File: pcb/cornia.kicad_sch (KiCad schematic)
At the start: 148 parts, among them J1 MJ-4PP-9, J2 OLED, J3 MJ-4PP-9, J4 OLED, SW1 SW_PUSH, SW10 SW_PUSH, SW11 SW_PUSH, SW12 SW_PUSH, SW13 SW_PUSH, SW14 SW_PUSH, SW15 SW_PUSH, SW16 SW_PUSH, SW17 SW_PUSH, SW18 SW_PUSH, SW19 SW_PUSH, SW2 SW_PUSH, SW20 SW_PUSH, SW21 SW_PUSH, SW22 SW_PUSH, SW23 SW_PUSH, SW24 SW_PUSH, SW25 SW_PUSH, SW26 SW_PUSH, SW27 SW_PUSH, SW28 SW_PUSH, SW29 SW_PUSH, SW3 SW_PUSH, SW30 SW_PUSH, SW31 SW_PUSH, SW32 SW_PUSH, SW33 SW_PUSH, SW34 SW_PUSH, SW35 SW_PUSH, SW36 SW_PUSH, SW37 SW_PUSH, SW38 SW_PUSH, SW39 SW_PUSH, SW4 SW_PUSH, SW40 SW_PUSH, SW41 SW_PUSH, SW42 SW_PUSH, SW5 SW_PUSH, SW6 SW_PUSH, SW7 SW_PUSH, SW8 SW_PUSH, SW9 SW_PUSH, U1 ProMicro, U2 ProMicro

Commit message: First push V1
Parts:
- removed D1, D10, D11, D12, D13, D14, D15, D16, D17, D18, D19, D2, D20, D21, D22, D23, D24, D25, D26, D27, D28, D29, D3, D30, D31, D32, D33, D34, D35, D36, D37, D38, D39, D4, D40, D41, D42, D5, D6, D7, D8, D9: D, Diode_SMD:D_MiniMELF, symbol Device:D
- removed J1, J3: MJ-4PP-9, kbd:MJ-4PP-9, symbol kbd:MJ-4PP-9
- removed J2, J4: OLED, kbd:OLED, symbol Connector_Generic:Conn_01x04
- removed LED1, LED2, LED28, LED29, LED3, LED30, LED31, LED32, LED33, LED4, LED5, LED6: WS2812B, LED_SMD:LED_WS2812B_PLCC4_5.0x5.0mm_P3.2mm, symbol LED:WS2812B
- removed LED10, LED11, LED12, LED13, LED14, LED15, LED16, LED17, LED18, LED19, LED20, LED21, LED22, LED23, LED24, LED25, LED26, LED27, LED34, LED35, LED36, LED37, LED38, LED39, LED40, LED41, LED42, LED43, LED44, LED45, LED46, LED47, LED48, LED49, LED50, LED51, LED52, LED53, LED54, LED7, LED8, LED9: YS-SK6812MINI-E, kbd:YS-SK6812MINI-E, symbol kbd:YS-SK6812MINI-E
- removed R1, R2: 0, Resistor_SMD:R_0603_1608Metric_Pad0.98x0.95mm_HandSolder, symbol Device:R
- removed RSW1, RSW2: SW_PUSH, kbd:ResetSW, symbol kbd:SW_PUSH
- removed SW1, SW10, SW11, SW12, SW13, SW14, SW15, SW16, SW17, SW18, SW19, SW2, SW20, SW21, SW22, SW23, SW24, SW25, SW26, SW27, SW28, SW29, SW3, SW30, SW31, SW32, SW33, SW34, SW35, SW36, SW37, SW38, SW39, SW4, SW40, SW41, SW42, SW5, SW6, SW7, SW8, SW9: SW_PUSH, kbd:keyswitch_cherrymx_hotswap_1u, symbol kbd:SW_PUSH
- removed U1, U2: ProMicro, kbd:ProMicro, symbol kbd:ProMicro
- added H1, H2, H3, H4, H5, H6: MountingHole, cornia-footprints:MountingHole_5mm, symbol Mechanical:MountingHole
- added JP6, JP7, JP8, JP9: SB, cornia-footprints:SolderJumper-3, symbol Jumper:SolderJumper_3_Open
- added L1, L10, L11, L12, L13, L14, L15, L16, L17, L18, L19, L2, L20, L21, L3, L4, L5, L6, L7, L8, L9: SK6812MINI, cornia-footprints:YS-SK6812MINI-E, symbol cornia:SK6812MINI
- added OL1: OLED, cornia-footprints:OLED, symbol cornia:OLED
- added RST_L1, RST_R1: SW_RST, cornia-footprints:SW_SMD_4x4mm, symbol Switch:SW_DIP_x01
- added SB1, SB3: SB, Jumper:SolderJumper-2_P1.3mm_Bridged_RoundedPad1.0x1.5mm, symbol Jumper:SolderJumper_2_Bridged
- added SB2: SB, Jumper:SolderJumper-2_P1.3mm_Open_RoundedPad1.0x1.5mm, symbol Jumper:SolderJumper_2_Open
- added SW1, SW10, SW11, SW12, SW13, SW14, SW15, SW16, SW17, SW18, SW19, SW2, SW20, SW21, SW3, SW4, SW5, SW6, SW7, SW8, SW9: SW_Push, cornia-footprints:keyswitch_cherrymx_hotswap_reversible_1u, symbol Switch:SW_Push
- added U1: RP2040-ProMicro, cornia-footprints:RP2040-ProMicro, symbol cornia:RP2040-ProMicro
- added U2: TRRS, cornia-footprints:TRRS, symbol cornia:TRRS
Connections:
- net GND: now also JP9.2 (C), L1.2 (VSS), L10.2 (VSS), L11.2 (VSS), L12.2 (VSS), L13.2 (VSS), L14.2 (VSS), L15.2 (VSS), L16.2 (VSS), L17.2 (VSS), L18.2 (VSS), L19.2 (VSS), L2.2 (VSS), L20.2 (VSS), L21.2 (VSS), L3.2 (VSS), L4.2 (VSS), L5.2 (VSS), L6.2 (VSS), L7.2 (VSS), L8.2 (VSS), L9.2 (VSS), RST_L1.2, RST_R1.2, SW1.2, SW10.2, SW11.2, SW12.2, SW13.2, SW14.2, SW15.2, SW16.2, SW17.2, SW18.2, SW19.2, SW2.2, SW20.2, SW21.2, SW3.2, SW4.2, SW5.2, SW6.2, SW7.2, SW8.2, SW9.2, U1.29 (GND), U1.4 (GND), U1.5 (GND), U2.4 (SLEEVE)
- net LED: now also L21.3 (DIN), SB3.2 (B)
- net SCL: now also JP7.2 (C), U1.31 (11)
- net SDA: now also JP6.2 (C), U1.1 (10)
- new net: L2.3 (DIN), L3.1 (DOUT)
- new net: L3.3 (DIN), L4.1 (DOUT)
- new net: L10.3 (DIN), L11.1 (DOUT)
- new net: L11.3 (DIN), L12.1 (DOUT)
- new net: L18.3 (DIN), L19.1 (DOUT)
- new net: L19.3 (DIN), L20.1 (DOUT)
- new net: L8.3 (DIN), L9.1 (DOUT)
- new net: L10.1 (DOUT), L9.3 (DIN)
- new net: L14.3 (DIN), L15.1 (DOUT)
- new net: L15.3 (DIN), L16.1 (DOUT)
- new net: L7.3 (DIN), L8.1 (DOUT)
- new net: JP6.3 (B), JP9.1 (A), OL1.4 (GND)
- new net: JP6.1 (A), JP9.3 (B), OL1.1 (SDA)
- new net: L12.3 (DIN), L13.1 (DOUT)
- new net: JP7.1 (A), JP8.3 (B), OL1.2 (SCL)
- new net: JP7.3 (B), JP8.1 (A), OL1.3 (VCC)
- new net: L16.3 (DIN), L17.1 (DOUT)
- new net: L17.3 (DIN), L18.1 (DOUT)
- new net: L5.3 (DIN), L6.1 (DOUT)
- new net: L6.3 (DIN), L7.1 (DOUT)
- new net: SB1.2 (B), U2.2 (RING1)
- new net: SB2.2 (B), U2.3 (RING2)
- new net: L20.3 (DIN), L21.1 (DOUT)
- new net: L4.3 (DIN), L5.1 (DOUT)
- new net: L13.3 (DIN), L14.1 (DOUT)
- new net: L1.3 (DIN), L2.1 (DOUT)
- new net In_SW1: SW1.1, U1.24 (27)
- new net In_SW10: SW10.1, U1.22
- new net In_SW11: SW11.1, U1.11 (7)
- new net In_SW12: SW12.1, U1.21 (20)
- new net In_SW13: SW13.1, U1.12 (8)
- new net In_SW14: SW14.1, U1.17 (15)
- new net In_SW15: SW15.1, U1.13 (9)
- new net In_SW16: SW16.1, U1.16 (14)
- new net In_SW17: SW17.1, U1.14 (12)
- new net In_SW18: SW18.1, U1.15 (13)
- new net In_SW19: SW19.1, U1.18 (16)
- new net In_SW2: SW2.1, U1.8 (4)
- new net In_SW20: SW20.1, U1.20 (23)
- new net In_SW21: SW21.1, U1.19 (21)
- new net In_SW3: SW3.1, U1.25 (28)
- new net In_SW4: SW4.1, U1.7 (3)
- new net In_SW5: SW5.1, U1.26 (29)
- new net In_SW6: SW6.1, U1.6 (2)
- new net In_SW7: SW7.1, U1.9 (5)
- new net In_SW8: SW8.1, U1.23 (26)
- new net In_SW9: SW9.1, U1.10 (6)
- new net RST: RST_L1.1, RST_R1.1, U1.28 (RST)
- new net RX_LED: SB2.1 (A), SB3.1 (A), U1.3 (RX1)
- new net TX: SB1.1 (A), U1.2 (TX0)
- new net VBUS: JP8.2 (C), L1.4 (VDD), L10.4 (VDD), L11.4 (VDD), L12.4 (VDD), L13.4 (VDD), L14.4 (VDD), L15.4 (VDD), L16.4 (VDD), L17.4 (VDD), L18.4 (VDD), L19.4 (VDD), L2.4 (VDD), L20.4 (VDD), L21.4 (VDD), L3.4 (VDD), L4.4 (VDD), L5.4 (VDD), L6.4 (VDD), L7.4 (VDD), L8.4 (VDD), L9.4 (VDD), U1.30 (VBUS), U2.1 (TIP)
- no-connect marks 14 -> 2
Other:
- company: vaarai -> (none)
- title: Corne Cherry -> (none)

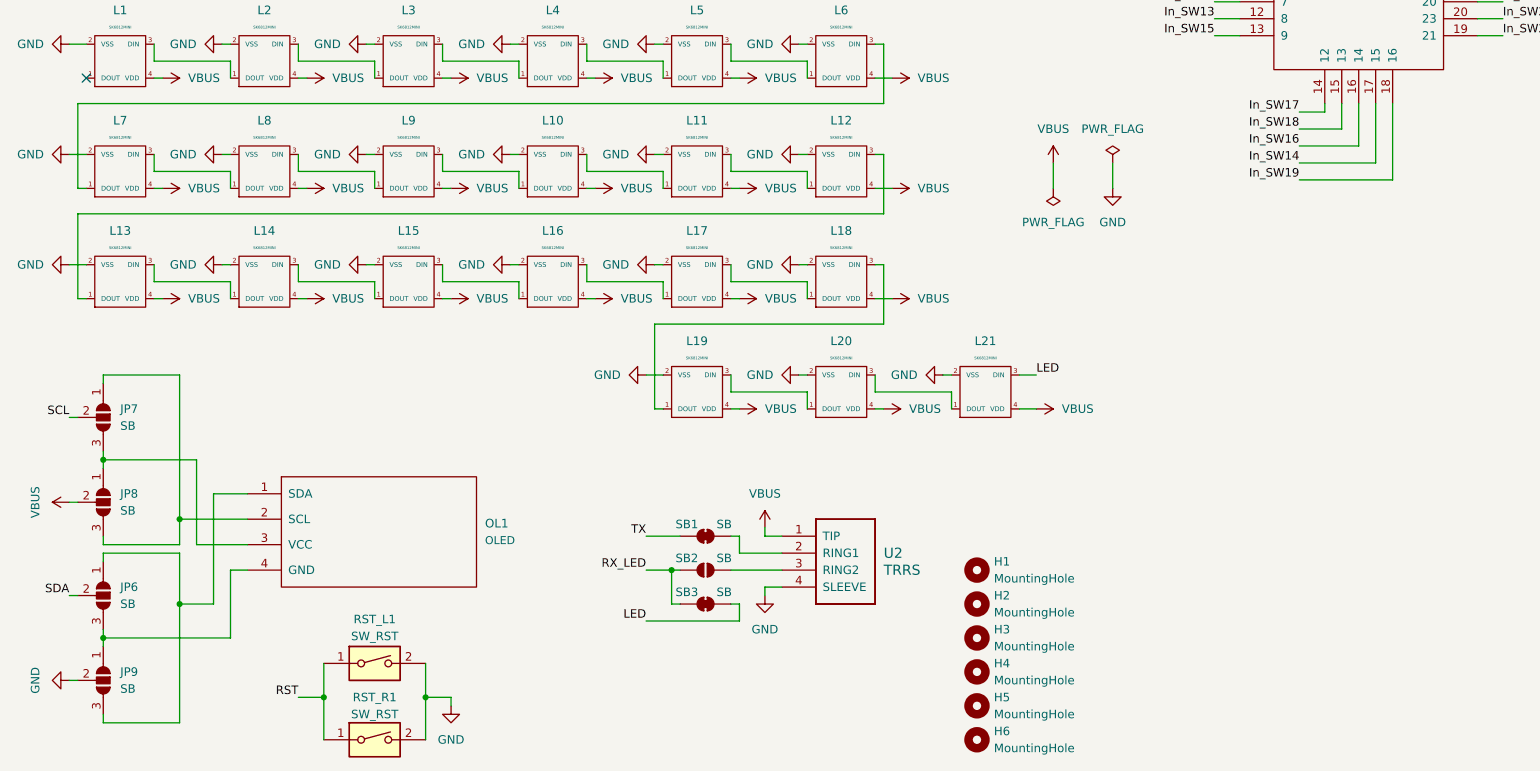
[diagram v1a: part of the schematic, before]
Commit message: Finish routing & add gerber/case export in CLI
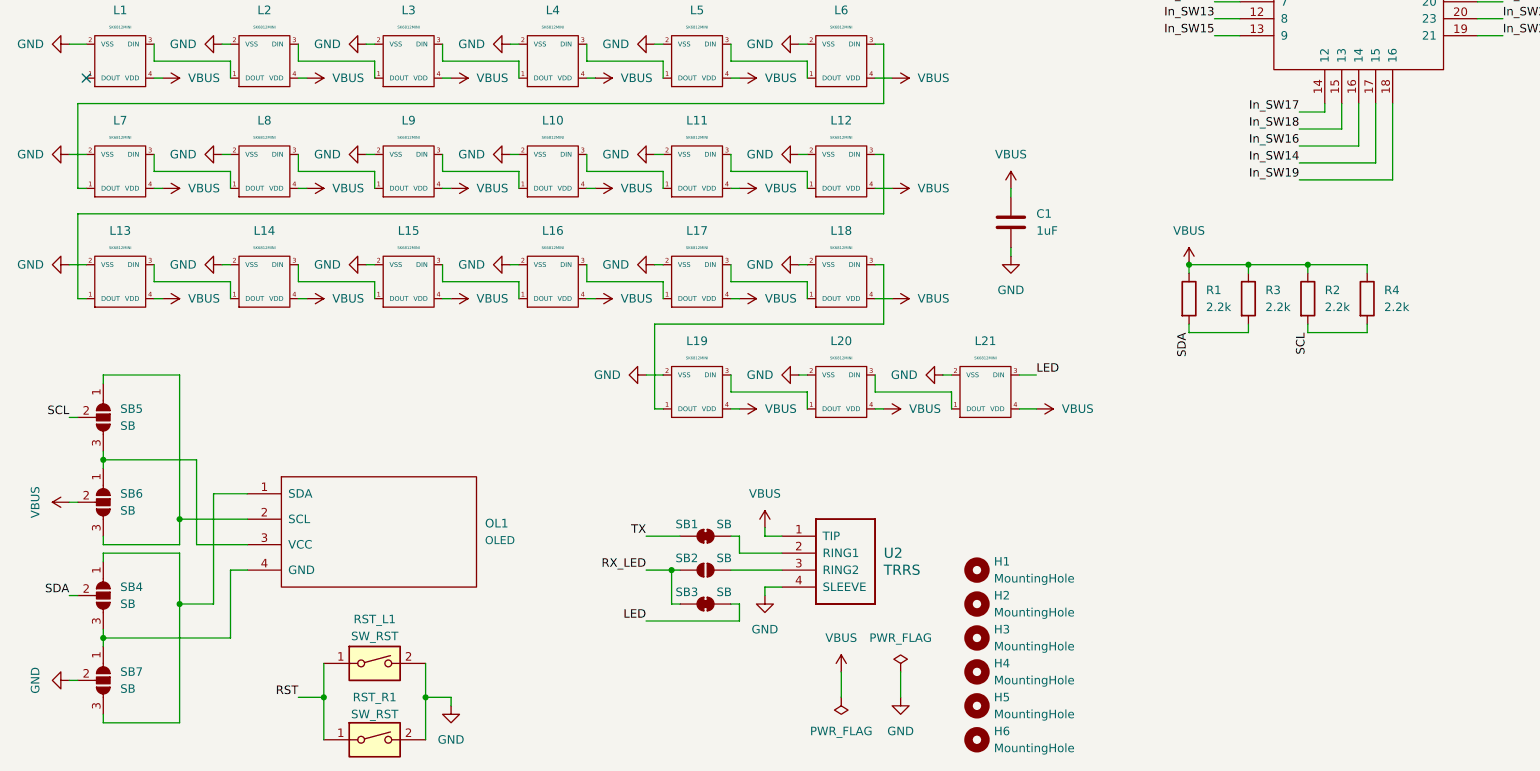
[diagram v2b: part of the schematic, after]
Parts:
- added C1: 1uF, cornia-footprints:C_0805, symbol Device:C
- added R1, R2, R3, R4: 2.2k, cornia-footprints:R_0805, symbol Device:R
- SB1, SB3: footprint Jumper:SolderJumper-2_P1.3mm_Bridged_RoundedPad1.0x1.5mm -> cornia-footprints:SolderJumper-2_Bridged
- SB2: footprint Jumper:SolderJumper-2_P1.3mm_Open_RoundedPad1.0x1.5mm -> cornia-footprints:SolderJumper-2_Open
- renumbered JP6 to SB4, JP7 to SB5, JP8 to SB6, JP9 to SB7
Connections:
- net GND: now also C1.2
- net SCL: now also R2.2, R4.2
- net SDA: now also R1.2, R3.2
- net VBUS: now also C1.1, R1.1, R2.1, R3.1, R4.1
